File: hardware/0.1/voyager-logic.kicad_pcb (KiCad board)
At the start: 6 copper layers, 50 x 50 mm, 159 parts, among them J201 USB_C_Receptacle, J401 JTAG, J402 JTAG, J501 Probe, SW401 KMR2, U201 TPD4EUSB30, U202 HD3SS3220, U203 TPD4EUSB30, U204 TPD4EUSB30, U301 CYUSB3014-BZXx, U302 M24M02, U501 SN74LVC245A, U502 SN74LVC245A, U701 TLV62569DRLR, U703 TLV62569DRLR, U704 TLV62569DRLR, Y301 19.2MHz

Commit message: usb3 routed less tuning
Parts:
- removed TP701, TP702, TP704, TP705: TP, josh-test-point:TestPoint_SMDPad_D0.5mm_NO_SILK
- removed TP703: TP, josh-test-point:S1751-46_smdTestPoint
- added D203: DESD5V0U1BL, josh-passives-smt:D_X1-DFN1006-2, F.Cu at (120.7, 98.6)
- added D204: DESD5V0U1BL, josh-passives-smt:D_X1-DFN1006-2, F.Cu at (119.6, 98.6)
- J401: value JTAG -> UART; footprint Connector:Tag-Connect_TC2030-IDC-NL_2x03_P1.27mm_Vertical -> josh-connectors:3_PIN_THT_Staggered
- J402: footprint Connector:Tag-Connect_TC2030-IDC-NL_2x03_P1.27mm_Vertical -> josh-connectors:6_PIN_THT_Staggered
- R205, R206, U204: moved to F.Cu
- U201: value TPD4EUSB30 -> USBLC6-2SC6; footprint Package_SON:USON-10_2.5x1.0mm_P0.5mm -> josh-soic-sot-etc:SOT-563
- moved J401 15.5 mm to (135.2, 71.9), turned to 90 degrees
- moved U201 9.26 mm to (123.9, 88.9)
- moved U204 1.60 mm to (119.5, 95.6), turned to 180 degrees
- moved U203 1.53 mm to (119.5, 92.5)
- moved C203 1.53 mm to (123.9, 94.4)
- moved C205 1.53 mm to (123.9, 95.1)
- moved C206 1.52 mm to (123.9, 91.8)
- moved C207 1.52 mm to (123.9, 92.5)
- moved J402 1.31 mm to (127.8, 71.9), turned to -90 degrees
- moved TP201 1.23 mm to (130.3, 90.5)
- moved R201 0.70 mm to (130.7, 98.4)
- moved R202 0.70 mm to (129.7, 98.4)
- moved R203 0.70 mm to (127.6, 98.3)
- moved R207 0.70 mm to (128.6, 98.3)
- moved U202 0.70 mm to (127.6, 94.1)
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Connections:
- H201 pad 1: Net-(C208-Pad1) -> GND
- H202 pad 1: unconnected-(H202-Pad1) -> GND
- H203 pad 1: unconnected-(H203-Pad1) -> GND
- H204 pad 1: unconnected-(H204-Pad1) -> GND
- J201 pad A10: /USB C Connector/TX1N -> /USB C Connector/RX2N
- J201 pad A11: /USB C Connector/TX1P -> /USB C Connector/RX2P
- J201 pad A2: /USB C Connector/RX2P -> /USB C Connector/TX1N
- J201 pad A3: /USB C Connector/RX2N -> /USB C Connector/TX1P
- J201 pad A6: /FX3 USB and Misc/USB2_D+ -> /USB C Connector/USBD+
- J201 pad A7: /FX3 USB and Misc/USB2_D- -> /USB C Connector/USBD-
- J201 pad B10: /USB C Connector/TX2N -> /USB C Connector/RX1P
- J201 pad B11: /USB C Connector/TX2P -> /USB C Connector/RX1N
- J201 pad B2: /USB C Connector/RX1P -> /USB C Connector/TX2P
- J201 pad B3: /USB C Connector/RX1N -> /USB C Connector/TX2N
- J201 pad B6: /FX3 USB and Misc/USB2_D+ -> /USB C Connector/USBD+
- J201 pad B7: /FX3 USB and Misc/USB2_D- -> /USB C Connector/USBD-
- U201 pad 1: /FX3 USB and Misc/USB2_D- -> /USB C Connector/USBD-
- U201 pad 2: /FX3 USB and Misc/USB2_D+ -> GND
- U201 pad 3: GND -> /USB C Connector/USBD+
- U201 pad 4: /USB C Connector/CC1 -> /FX3 USB and Misc/USB2_D+
- U201 pad 5: /USB C Connector/CC2 -> VBUS
- U201 pad 6: unconnected-(U201-Pad6) -> /FX3 USB and Misc/USB2_D-
- U203 pad 10: unconnected-(U203-Pad10) -> /USB C Connector/TX1P
- U203 pad 4: /USB C Connector/RX2N -> /USB C Connector/RX1P
- U203 pad 5: /USB C Connector/RX2P -> /USB C Connector/RX1N
- U203 pad 6: unconnected-(U203-Pad6) -> /USB C Connector/RX1N
- U203 pad 7: unconnected-(U203-Pad7) -> /USB C Connector/RX1P
- U203 pad 9: unconnected-(U203-Pad9) -> /USB C Connector/TX1N
- U204 pad 1: /USB C Connector/RX1P -> /USB C Connector/TX2P
- U204 pad 10: unconnected-(U204-Pad10) -> /USB C Connector/TX2P
- U204 pad 2: /USB C Connector/RX1N -> /USB C Connector/TX2N
- U204 pad 4: /USB C Connector/TX2N -> /USB C Connector/RX2P
- U204 pad 5: /USB C Connector/TX2P -> /USB C Connector/RX2N
- U204 pad 6: unconnected-(U204-Pad6) -> /USB C Connector/RX2N
- U204 pad 7: unconnected-(U204-Pad7) -> /USB C Connector/RX2P
- U204 pad 9: unconnected-(U204-Pad9) -> /USB C Connector/TX2N
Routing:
- net /USB C Connector/RX1N: track 0.00 -> 15.5 mm, vias 0 -> 1
- net /USB C Connector/RX1P: track 0.00 -> 14.9 mm, vias 0 -> 1
- net /USB C Connector/RX2P: track 0.00 -> 12.3 mm
- net /USB C Connector/RX2N: track 0.00 -> 12.3 mm
- net /USB C Connector/TX2P: track 0.00 -> 12.0 mm, vias 0 -> 1
- net /USB C Connector/TX2N: track 0.00 -> 11.8 mm, vias 0 -> 1
- net /USB C Connector/TX1N: track 0.00 -> 9.75 mm
- net /USB C Connector/TX1P: track 0.00 -> 9.75 mm
- net GND: track 57.3 -> 64.9 mm, vias 36 -> 41
- net /USB C Connector/USBD-: track 0.00 -> 3.14 mm, vias 0 -> 1
- net /USB C Connector/TX1+: track 0.00 -> 3.05 mm
- net /USB C Connector/TX1-: track 0.00 -> 2.90 mm
- net VBUS: track 0.00 -> 2.66 mm
- net /USB C Connector/TX2-: track 0.00 -> 2.53 mm
- net /USB C Connector/TX2+: track 0.00 -> 2.53 mm
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
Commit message: wip, switchers todo
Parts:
- added G***: LOGO, LOGO, B.Cu at (120.4, 81.9)
- added kibuzzard-63948718: G***, kibuzzard-63948718, F.Cu at (123.0, 79.1)
- D502, D504, D505, D508, D509, D512, D513, D516, R504, R506, R507, R510, R512, R515, R517, R520: moved to B.Cu
- moved J401 43.5 mm to (130.2, 115.1)
- moved R405 30.1 mm to (112.5, 108.7), turned to -90 degrees
- moved R406 29.2 mm to (111.5, 108.7), turned to -90 degrees
- moved R407 28.3 mm to (110.5, 108.7), turned to -90 degrees
- moved D402 26.9 mm to (111.5, 106.5), turned to 180 degrees
- moved R402 14.7 mm to (111.8, 84.9), turned to 0 degrees
- moved SW401 10.3 mm to (111.5, 81.5), turned to 90 degrees
- moved D512 8.30 mm to (149.2, 106.3), turned to 180 degrees
- moved L702 8.25 mm to (120.6, 114.5), turned to -90 degrees
- moved R515 7.66 mm to (148.9, 107.3), turned to 180 degrees
- moved R408 7.17 mm to (136.7, 75.7)
- moved C721 7.07 mm to (123.0, 115.5), turned to 0 degrees
- moved R506 7.04 mm to (145.8, 107.3), turned to 180 degrees
- moved D504 6.96 mm to (146.1, 106.3), turned to 180 degrees
- moved D516 6.84 mm to (150.7, 108.8), turned to 180 degrees
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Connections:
- net Net-(C208-Pad1) renamed /USB C Connector/SHIELD
- J401 pad 1: /Debug/UART_TX -> GND
- J401 pad 3: GND -> /Debug/UART_TX
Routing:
- net GND: track 64.9 -> 117.2 mm, vias 41 -> 149
- net /Debug/FX3_NRST: track 10.1 -> 42.9 mm, vias 1 -> 2
- net /Logic Front End/CHANNEL_14: track 0.00 -> 31.1 mm, vias 0 -> 1
- net /Logic Front End/CHANNEL_15: track 0.00 -> 30.6 mm
- net /Debug/JTAG_TDO: track 2.15 -> 31.2 mm
- net /Logic Front End/CHANNEL_13: track 0.00 -> 28.9 mm, vias 0 -> 1
- net /Logic Front End/CHANNEL_10: track 0.00 -> 28.8 mm
- net /Logic Front End/CHANNEL_0: track 0.00 -> 27.4 mm, vias 0 -> 1
- net /Logic Front End/CHANNEL_9: track 0.00 -> 27.1 mm
- net /Logic Front End/CHANNEL_8: track 0.00 -> 26.5 mm
- net /Logic Front End/CHANNEL_12: track 0.00 -> 26.4 mm, vias 0 -> 1
- net /Logic Front End/CHANNEL_4: track 0.00 -> 26.2 mm
- net /Logic Front End/CHANNEL_1: track 0.00 -> 25.8 mm, vias 0 -> 1
- net +5V: track 9.86 -> 35.4 mm, vias 2 -> 3
- net VBUS: track 2.66 -> 27.8 mm, vias 0 -> 3
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- added copper zone on F.Cu, net /USB C Connector/SHIELD
- added copper zone on B.Cu, net GND
- added copper zone on F.Cu, net GND
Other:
- board text added: "1"
- board text added: "2"
- board text added: "3"
- board text added: "4"
- board text added: "5"
- board text added: "6"
- board text added: "<TX"
- board text added: ">RX"
- board text added: "Born too late to explore the earth Born too soon to explore the galaxy Born just in time to view ones and zeros"
- board text added: "GND"
- board text added: "Josh Johnson R0.1 12/22"
- board text added: "PWR"
- board text added: "RST"
- board text added: "TCK"
- board text added: "TDI"
- board text added: "TDO"
- board text added: "TMS"
- board text added: "TRST"

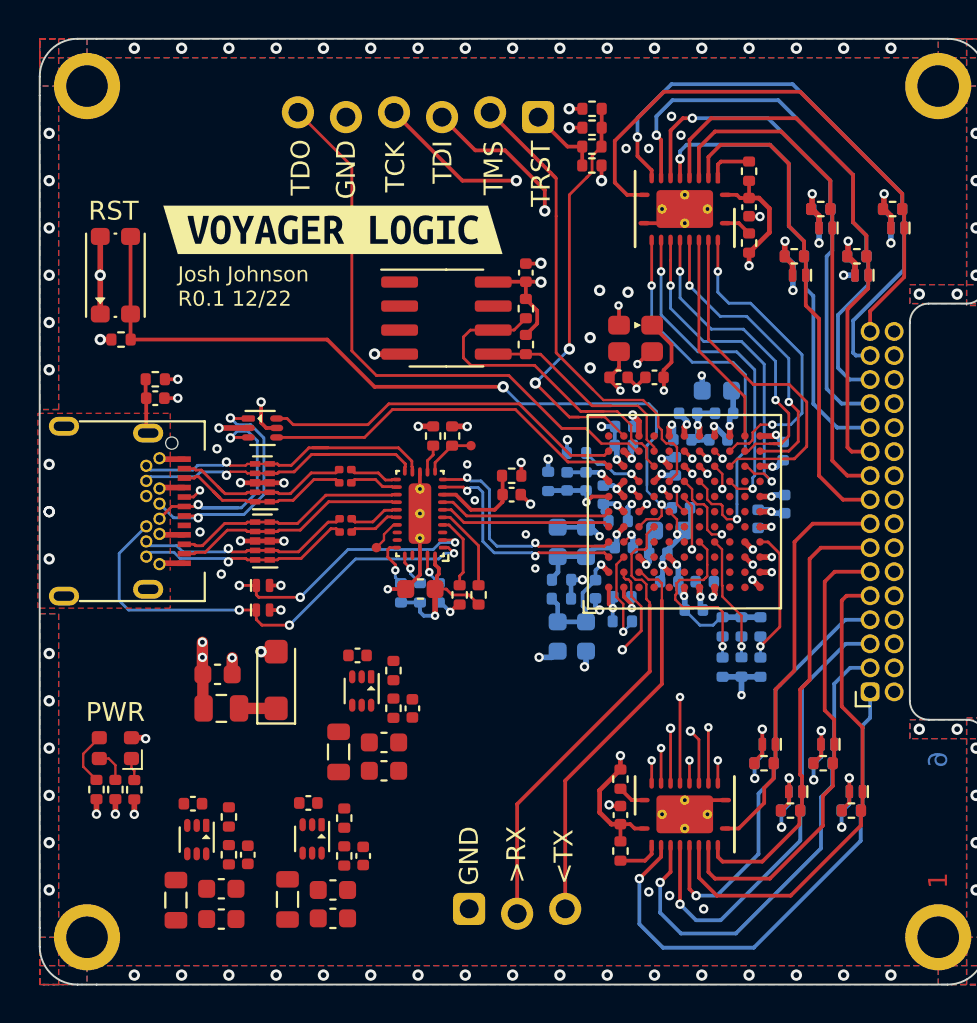
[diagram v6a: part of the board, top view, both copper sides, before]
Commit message: erc = drc = 0, fixup BOM
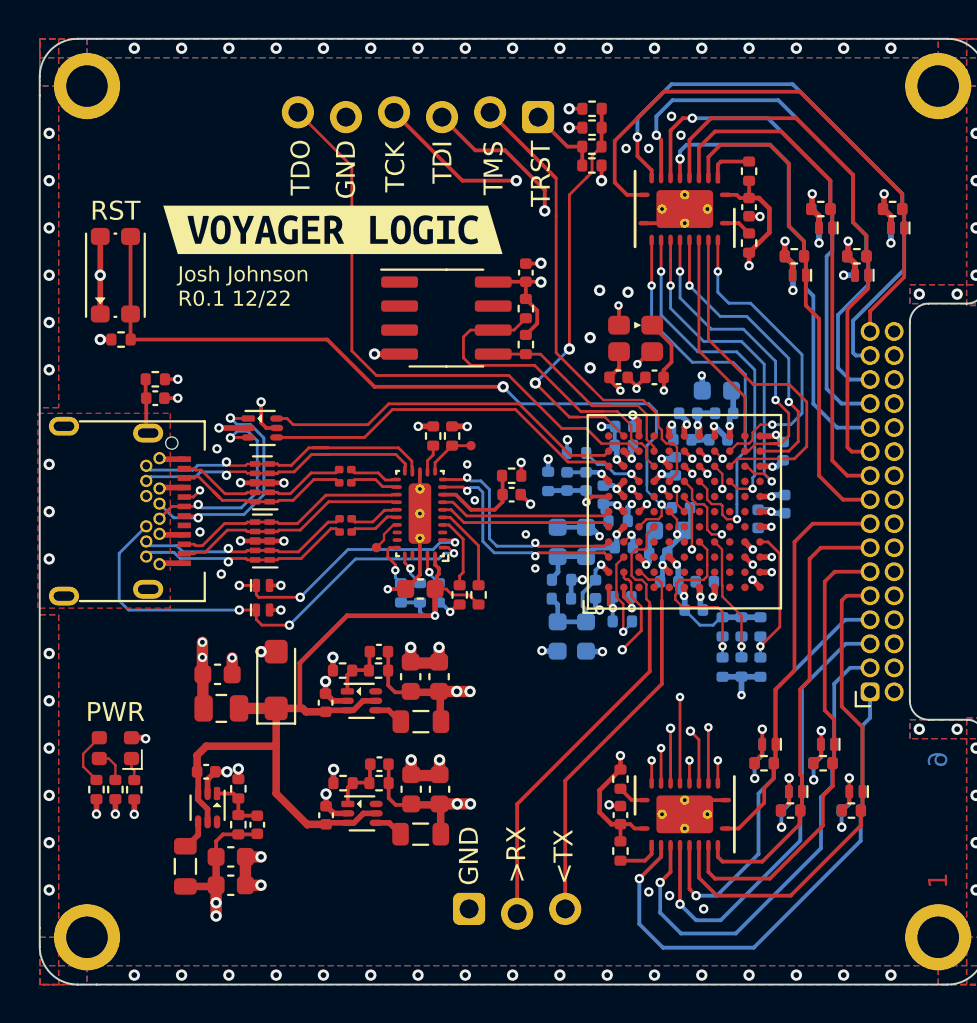
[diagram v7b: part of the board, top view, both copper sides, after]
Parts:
- R409: value 0R0 -> 0R
- U201: value USBLC6-2SC6 -> USBLC6-2P6
- moved C721 14.0 mm to (128.6, 102.7), turned to 90 degrees
- moved C722 12.0 mm to (127.1, 102.7), turned to 90 degrees
- moved L702 11.8 mm to (127.7, 105.1), turned to 0 degrees
- moved C723 10.8 mm to (125.4, 101.4), turned to 180 degrees
- moved R703 9.97 mm to (125.4, 102.4), turned to 180 degrees
- moved C737 8.61 mm to (122.6, 110.0), turned to 90 degrees
- moved R704 7.80 mm to (123.5, 102.4), turned to 180 degrees
- moved U703 7.75 mm to (124.5, 104.0), turned to 0 degrees
- moved R706 6.52 mm to (123.5, 108.3), turned to 180 degrees
- moved U704 6.47 mm to (124.5, 110.0), turned to 0 degrees
- moved L703 6.14 mm to (127.6, 111.0), turned to 0 degrees
- moved C724 5.38 mm to (122.6, 104.1), turned to 90 degrees
- moved R705 4.03 mm to (125.4, 108.3), turned to 180 degrees
- moved C736 3.43 mm to (125.5, 107.3), turned to 180 degrees
- moved C734 3.10 mm to (128.6, 108.7), turned to 90 degrees
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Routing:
- net +5V: track 35.4 -> 70.4 mm
- net VIO: track 65.2 -> 82.7 mm, vias 6 -> 8
- net +1V2: track 15.6 -> 33.1 mm, vias 10 -> 12
- net GND: track 117.2 -> 133.8 mm, vias 149 -> 160
- net +3V3: track 20.6 -> 27.8 mm, vias 9 -> 11
- net Net-(C736-Pad2): track 0.00 -> 3.13 mm
- net Net-(C723-Pad2): track 0.00 -> 3.13 mm
- net Net-(C703-Pad2): track 0.00 -> 3.13 mm
- net /USB C Connector/USBD-: track 15.4 -> 13.3 mm
- net /USB C Connector/USBD+: track 13.3 -> 11.3 mm
- net Net-(L703-Pad1): track 0.00 -> 1.54 mm
- net Net-(L702-Pad1): track 0.00 -> 1.54 mm
- net Net-(L701-Pad1): track 0.00 -> 1.54 mm

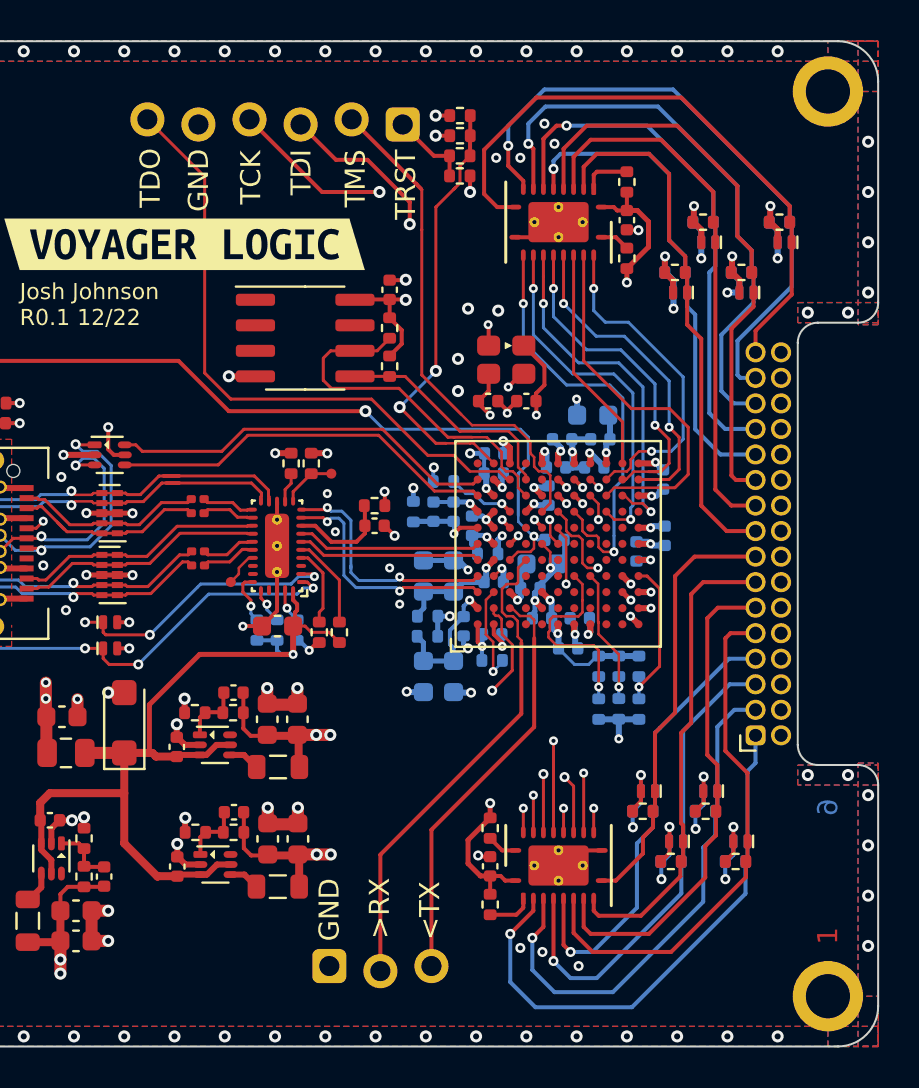
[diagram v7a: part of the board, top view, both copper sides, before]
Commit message: component shortage changes
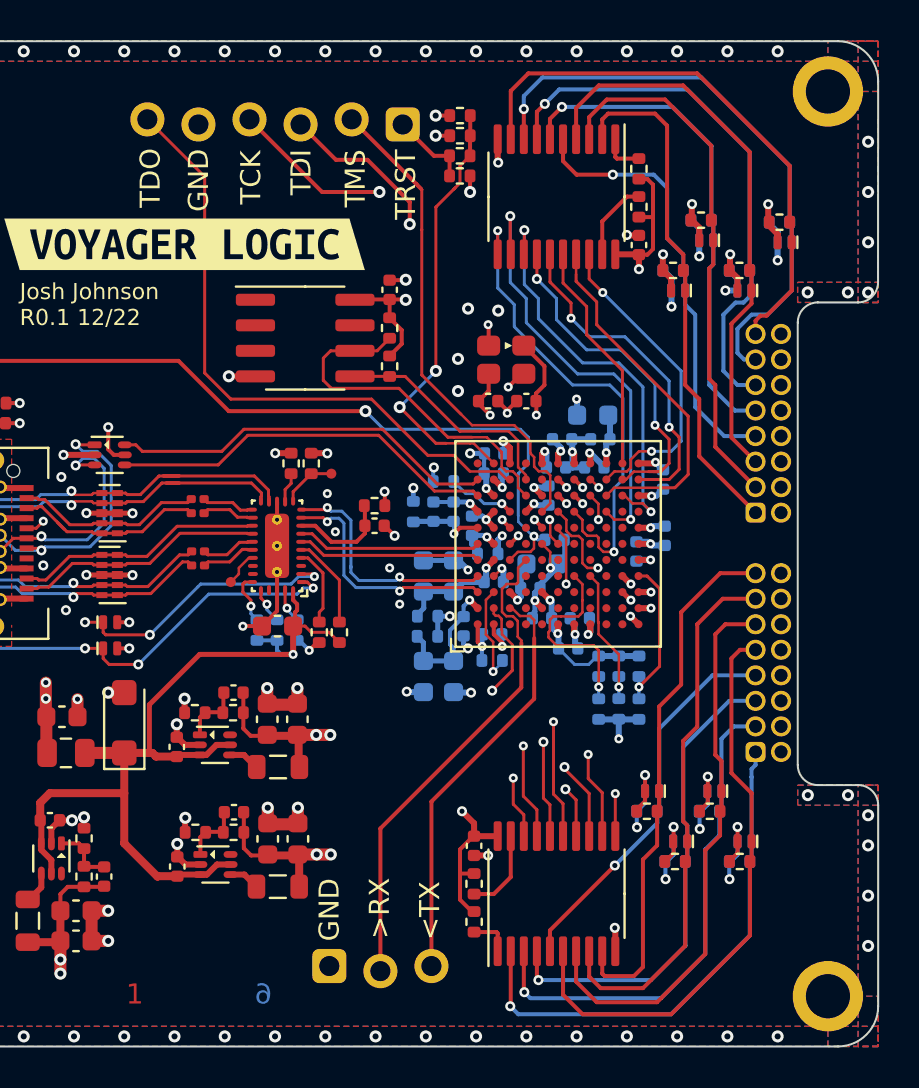
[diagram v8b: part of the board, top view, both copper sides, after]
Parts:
- added J502: Probe, josh-connectors:PinSocket_2x08_P1.27mm_Horizontal, F.Cu at (151.4, 92.5)
- J501: footprint josh-connectors:PinSocket_2x16_P1.27mm_Horizontal -> josh-connectors:PinSocket_2x08_P1.27mm_Horizontal
- U501, U502: footprint josh-dfn-qfn:Texas_RGY0020A_VQFN-20_2.5x4.5mm_P0.5mm -> Package_SO:TSSOP-20_4.4x6.5mm_P0.65mm
- moved R502 2.88 mm to (137.4, 110.9)
- moved R516 2.63 mm to (145.6, 77.2)
- moved U501 1.40 mm to (141.5, 111.4)
- moved C502 1.38 mm to (145.6, 79.1), turned to 90 degrees
- moved C501 1.30 mm to (137.4, 109.0), turned to -90 degrees
- moved U502 1.27 mm to (141.5, 76.7)
- moved R501 1.17 mm to (137.4, 112.8)
- moved R511 0.89 mm to (145.6, 75.3)
- moved J501 0.82 mm to (151.4, 104.3)
- moved D507 0.21 mm to (147.7, 108.8)
- moved D508 0.21 mm to (147.7, 108.8)
- moved R505 0.21 mm to (146.0, 107.3)
- moved R509 0.21 mm to (147.4, 109.8)
- moved R510 0.21 mm to (147.4, 109.8)
- moved R514 0.21 mm to (149.1, 107.3)
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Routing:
- net /Logic Front End/CHANNEL_7: track 21.5 -> 26.3 mm
- net /FX3 Logic Inputs/CH_14: track 17.8 -> 21.9 mm
- net /Logic Front End/CHANNEL_3: track 22.7 -> 19.2 mm
- net /Logic Front End/CHANNEL_6: track 23.6 -> 27.0 mm
- net /Logic Front End/CHANNEL_5: track 24.7 -> 27.9 mm
- net /Logic Front End/CHANNEL_4: track 26.2 -> 29.1 mm
- net /Logic Front End/CHANNEL_15: track 30.6 -> 27.7 mm
- net /FX3 Logic Inputs/CH_15: track 21.7 -> 24.4 mm
- net /FX3 Logic Inputs/CH_13: track 17.8 -> 20.5 mm
- net Net-(R502-Pad2): track 1.50 -> 4.21 mm
- net GND: track 133.8 -> 131.1 mm, vias 160 -> 155
- net /Logic Front End/CHANNEL_11: track 24.5 -> 21.9 mm
- net Net-(R516-Pad2): track 1.47 -> 3.97 mm
- net VIO: track 82.7 -> 84.8 mm
- net /Logic Front End/CHANNEL_14: track 31.1 -> 29.4 mm
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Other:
- outline, holes or cut-outs redrawn
